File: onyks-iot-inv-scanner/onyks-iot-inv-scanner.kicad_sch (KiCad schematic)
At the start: 19 parts, among them J1 Conn_01x24_MountingPin, J2 USB_C_Receptacle, SW1 EN, SW2 BOOT, U2 ESP32-S3-WROOM-1

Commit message: added 3v3 dc-dc converter
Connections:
- net AGND is gone; now on net GND: J1.23 (Pin_23)
- net DGND is gone; now on net GND: J1.10 (Pin_10)
- net VCC5V renamed VUSB
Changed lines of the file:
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@@
 	(rectangle
 		(start 13.97 13.97)
-		(end 40.64 93.98)
+		(end 57.15 93.98)
 		(stroke
 			(width 0)
@@
 		(color 0 0 0 0)
 	)
+	(junction
+		(at 48.26 25.4)
+		(diameter 0)
+		(color 0 0 0 0)
+	)
 	(wire
 		(pts
@@
 	(wire
 		(pts
+			(xy 39.37 22.86) (xy 48.26 22.86)
+		)
+		(stroke
+			(width 0)
+			(type default)
+		)
+	)
+	(wire
+		(pts
 			(xy 265.43 52.07) (xy 275.59 52.07)
 		)
@@
 	(wire
 		(pts
+			(xy 48.26 22.86) (xy 48.26 25.4)
+		)
+		(stroke
+			(width 0)
+			(type default)
+		)
+	)
+	(wire
+		(pts
 			(xy 265.43 34.29) (xy 275.59 34.29)
 		)
@@
 	(wire
 		(pts
+			(xy 39.37 25.4) (xy 48.26 25.4)
+		)
+		(stroke
+			(width 0)
+			(type default)
+		)
+	)
+	(wire
+		(pts
 			(xy 19.05 60.96) (xy 27.94 60.96)
 		)
@@
 	(wire
 		(pts
+			(xy 48.26 25.4) (xy 53.34 25.4)
+		)
+		(stroke
+			(width 0)
+			(type default)
+		)
+	)
+	(wire
+		(pts
 			(xy 228.6 57.15) (xy 234.95 57.15)
 		)
@@
 	(wire
 		(pts
+			(xy 53.34 27.94) (xy 53.34 25.4)
+		)
+		(stroke
+			(width 0)
+			(type default)
+		)
+	)
+	(wire
+		(pts
 			(xy 228.6 54.61) (xy 234.95 54.61)
 		)
@@
 		)
 	)
+	(label "DGND"
+		(at 39.37 22.86 0)
+		(effects
+			(font
+				(size 1.27 1.27)
+			)
+			(justify left bottom)
+		)
+	)
 	(label "AGND"
 		(at 19.05 78.74 0)
@@
 		)
 	)
+	(label "AGND"
+		(at 39.37 25.4 0)
+		(effects
+			(font
+				(size 1.27 1.27)
+			)
+			(justify left bottom)
+		)
+	)
 	(label "IO16"
 		(at 228.6 80.01 0)
@@
 	)
 	(symbol
+		(lib_id "power:GND")
+		(at 53.34 27.94 0)
+		(unit 1)
+		(exclude_from_sim no)
+		(in_bom yes)
+		(on_board yes)
+		(dnp no)
+		(fields_autoplaced yes)
+		(property "Reference" "#PWR032"
+			(at 53.34 34.29 0)
+			(effects
+				(font
+					(size 1.27 1.27)
+				)
+				(hide yes)
+			)
+		)
+		(property "Value" "GND"
+			(at 53.34 33.02 0)
+			(effects
+				(font
+					(size 1.27 1.27)
+				)
+			)
+		)
+		(property "Footprint" ""
+			(at 53.34 27.94 0)
+			(effects
+				(font
+					(size 1.27 1.27)
+				)
+				(hide yes)
+			)
+		)
+		(property "Datasheet" ""
+			(at 53.34 27.94 0)
+			(effects
+				(font
+					(size 1.27 1.27)
+				)
+				(hide yes)
+			)
+		)
+		(property "Description" "Power symbol creates a global label with name \"GND\" , ground"
+			(at 53.34 27.94 0)
+			(effects
+				(font
+					(size 1.27 1.27)
+				)
+				(hide yes)
+			)
+		)
+		(pin "1"
+		)
+		(instances
+			(project ""
+				(path "/37956750-1b3c-4b3f-94c5-40fd1631cd50"
+					(reference "#PWR032")
+					(unit 1)
+				)
+			)
+		)
+	)
+	(symbol
 		(lib_id "Device:R")
 		(at 172.72 38.1 90)
@@
 			)
 		)
-		(property "Value" "VCC5V"
+		(property "Value" "VUSB"
 			(at 69.85 111.76 0)
 			(effects
@@
 	)
 	(sheet
-		(at 46.99 17.78)
+		(at 59.69 16.51)
 		(size 24.13 13.97)
 		(exclude_from_sim no)
@@
 		)
 		(property "Sheetname" "Power Supply"
-			(at 46.99 17.0684 0)
+			(at 59.69 15.7984 0)
 			(effects
 				(font
@@
 		)
 		(property "Sheetfile" "power_supply.kicad_sch"
-			(at 46.99 32.3346 0)
+			(at 59.69 31.0646 0)
 			(effects
 				(font
@@
 		)
 		(pin "BAT_SENSE" output
-			(at 71.12 20.32 0)
+			(at 83.82 19.05 0)
 			(effects
 				(font

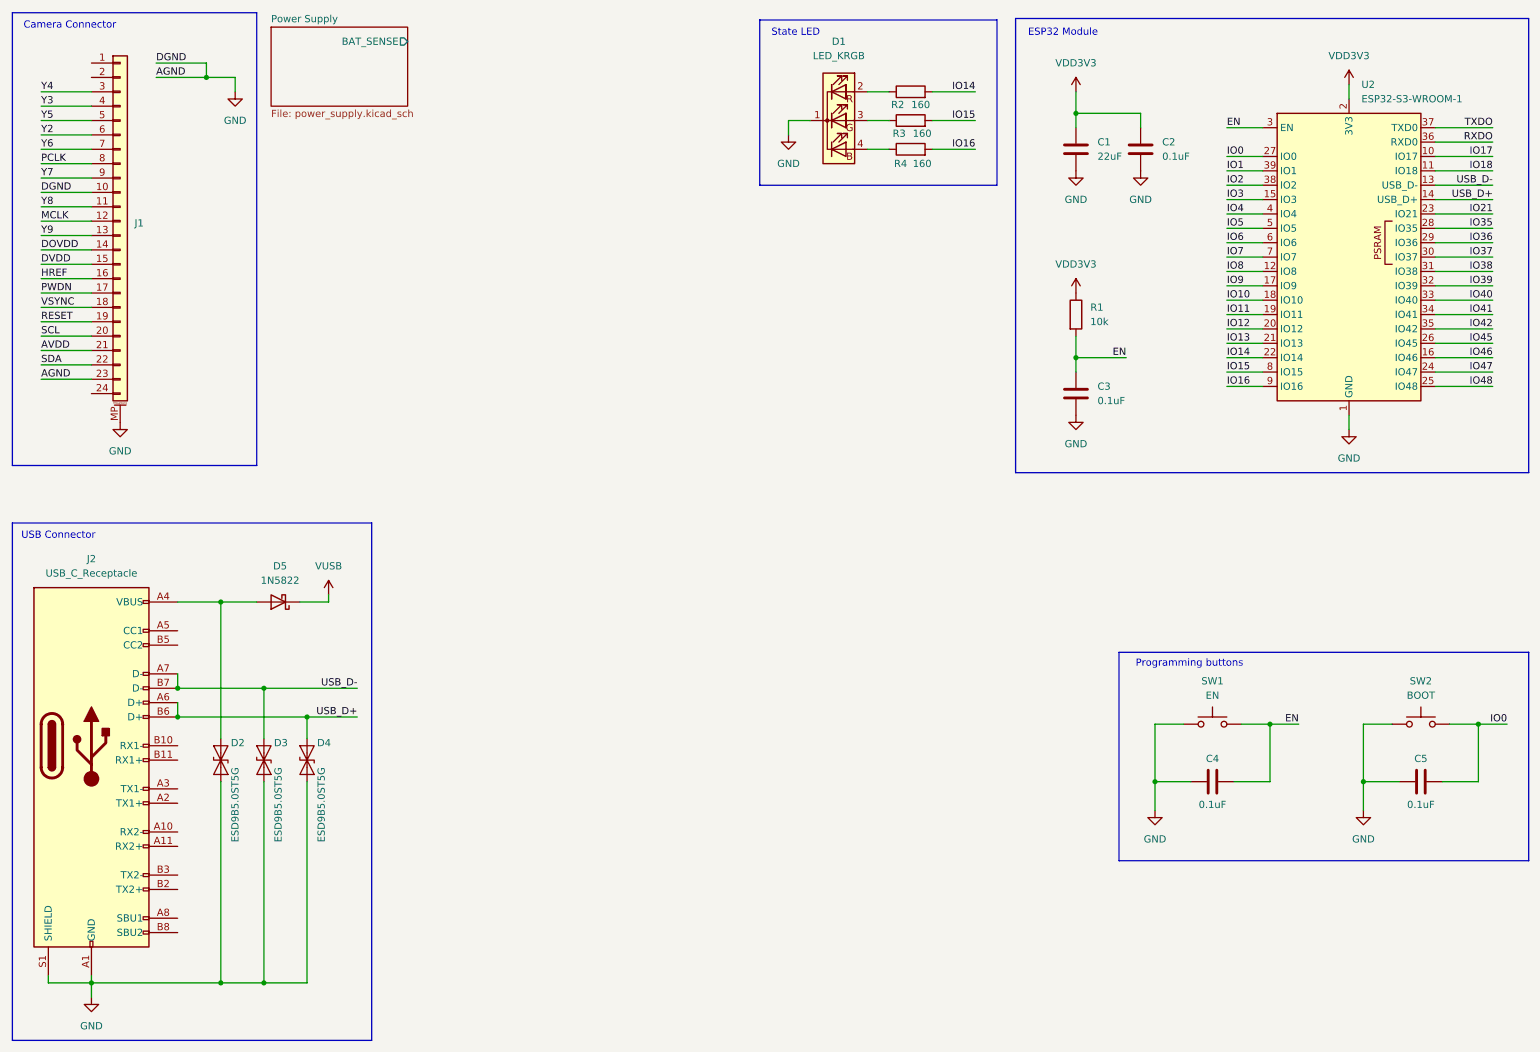
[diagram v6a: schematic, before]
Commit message: added display support
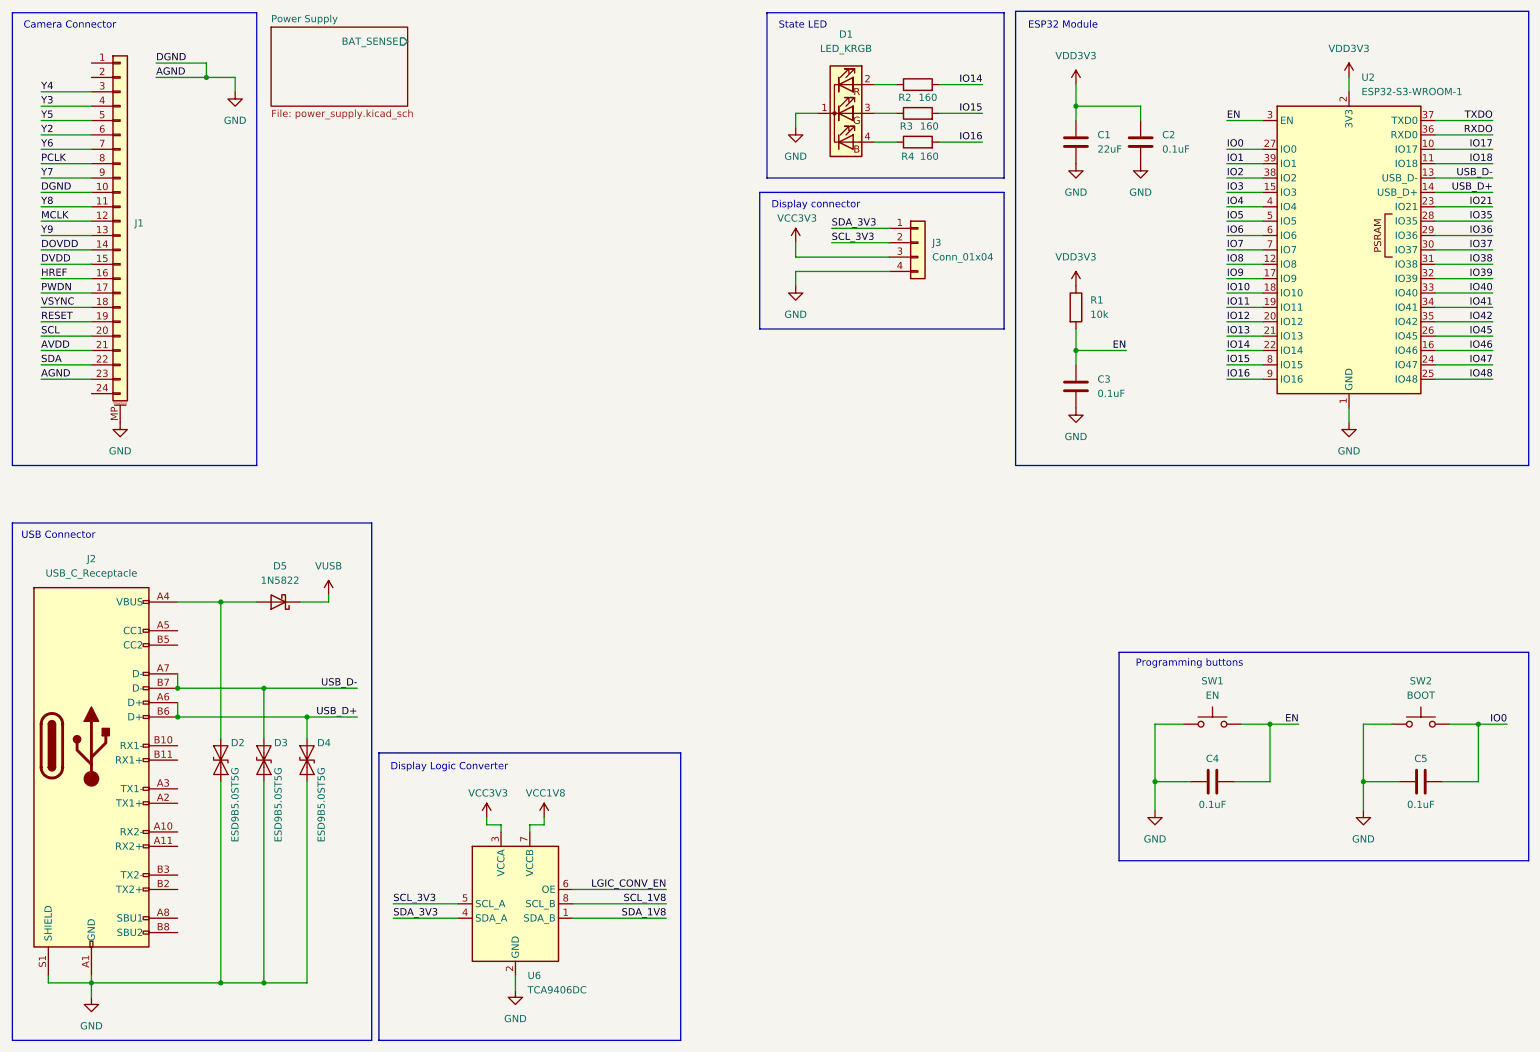
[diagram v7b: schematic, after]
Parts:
- added J3: Conn_01x04, symbol Connector_Generic:Conn_01x04
- added U6: TCA9406DC, symbol Interface:TCA9406DC
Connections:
- net GND: now also J3.4 (Pin_4), U6.2 (GND)
- new net LGIC_CONV_EN: U6.6 (OE)
- new net SCL_1V8: U6.8 (SCL_B)
- new net SCL_3V3: J3.2 (Pin_2), U6.5 (SCL_A)
- new net SDA_1V8: U6.1 (SDA_B)
- new net SDA_3V3: J3.1 (Pin_1), U6.4 (SDA_A)
- new net VCC1V8: U6.7 (VCCB)
- new net VCC3V3: J3.3 (Pin_3), U6.3 (VCCA)
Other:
- note added: "Display Logic Converter"
- note added: "Display connector"
- moved on the sheet: C1, C2, C3, D1, R1, R2, R3, R4, U2

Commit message: net labels correction and connected batsense
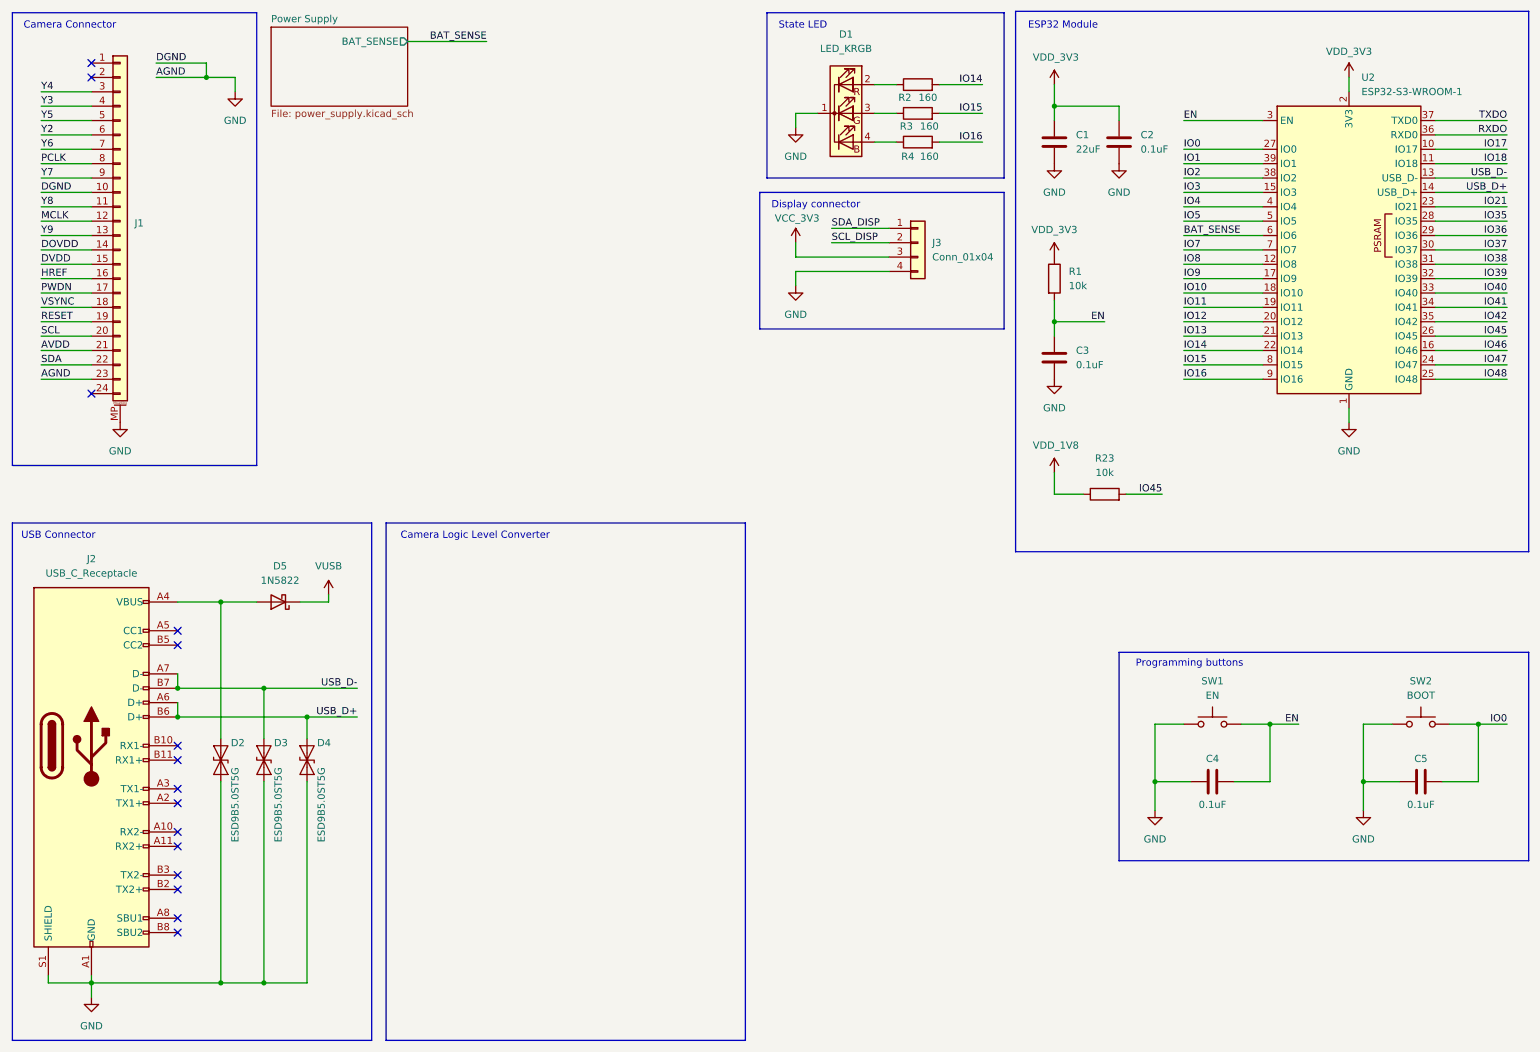
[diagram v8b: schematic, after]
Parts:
- removed U6: TCA9406DC, symbol Interface:TCA9406DC
- added R23: 10k, symbol Device:R
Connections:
- net IO45: now also R23.2
- net IO6 renamed BAT_SENSE
- net SCL_3V3 renamed SCL_DISP
- net SDA_3V3 renamed SDA_DISP
- net VCC3V3 renamed VCC_3V3
- net VDD3V3 renamed VDD_3V3
- new net VDD_1V8: R23.1
- no-connect marks 0 -> 15
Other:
- note added: "Camera Logic Level Converter"
- note removed: "Display Logic Converter"
- moved on the sheet: C1, C2, C3, R1
